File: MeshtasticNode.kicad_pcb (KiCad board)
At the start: 4 copper layers, 71.3 x 72.8 mm, 39 parts, among them J1 Conn_01x02_Socket, J2 Conn_01x02_Socket, J3 Conn_01x04_Socket, J4 Conn_01x03_Pin, J5 Conn_01x03_Pin, J6 Conn_01x03_Pin, J8 Conn_01x03_Pin, U1 BQ24074, U2 HT-CT62, U8 XC6206PxxxMR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

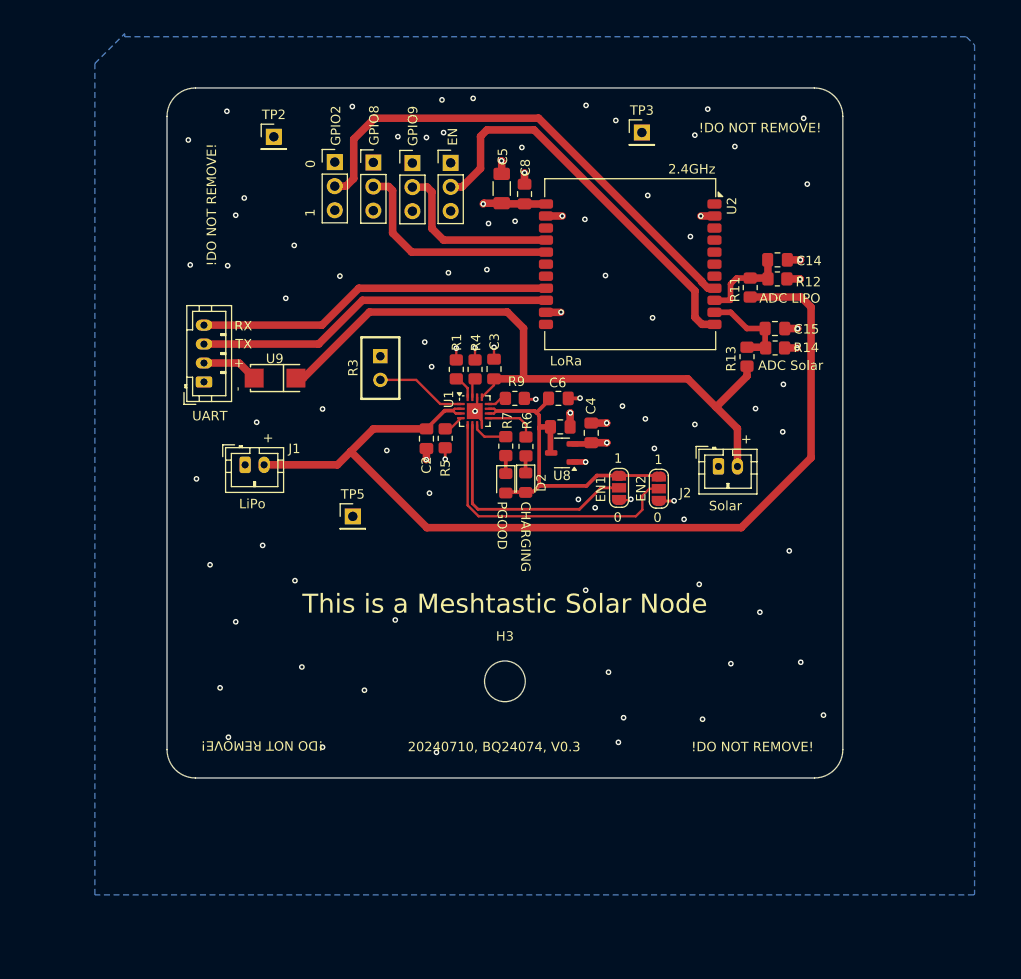
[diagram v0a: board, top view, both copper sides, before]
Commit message: pcb: add I2C port and remove a few warnings from EN1/EN2 solder switches
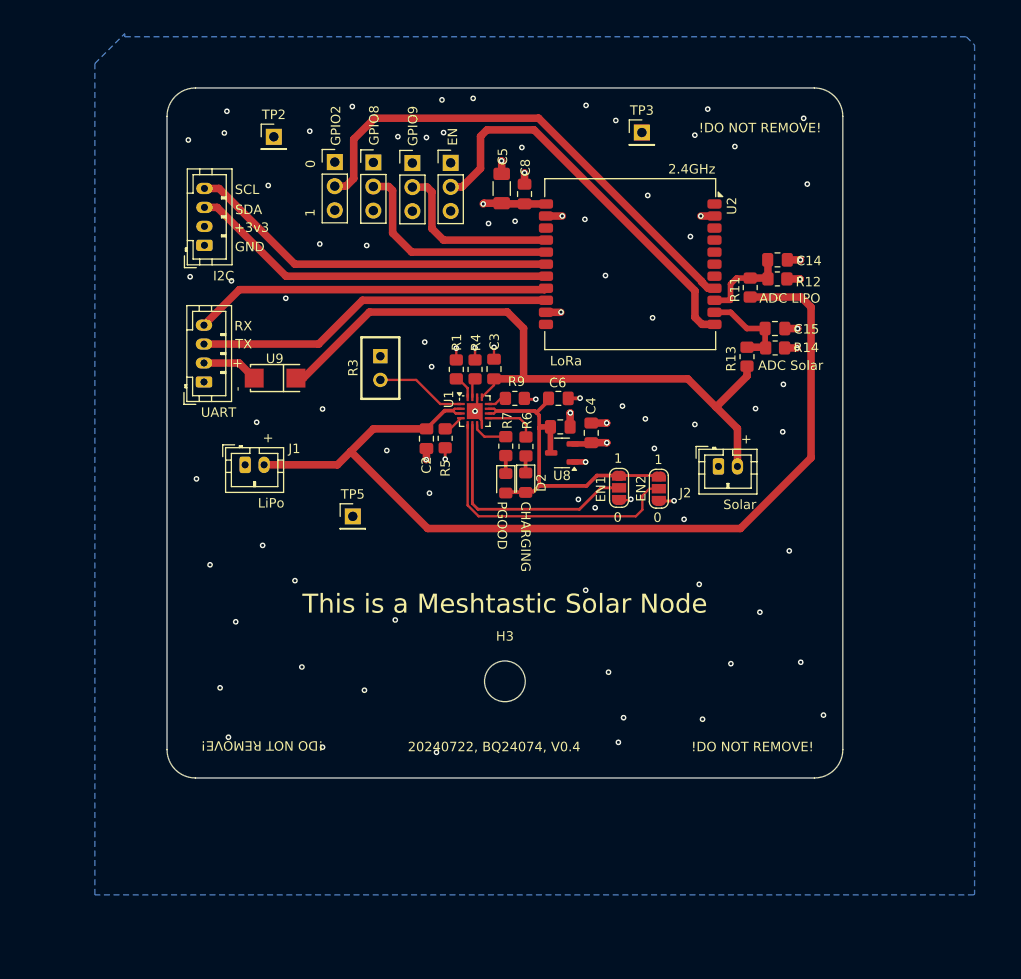
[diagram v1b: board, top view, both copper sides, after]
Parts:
- added J7: Conn_01x04_Socket, Connector_JST:JST_PH_B4B-PH-K_1x04_P2.00mm_Vertical, F.Cu at (187.1, 45.9)
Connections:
- U2 pad 17: /USB_D- -> /I2C_SCL
- U2 pad 18: /USB_D+ -> /I2C_SDA
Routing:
- net /I2C_SCL: track 0.00 -> 39.3 mm
- net /I2C_SDA: track 0.00 -> 39.0 mm
- net GND: vias 93 -> 92
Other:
- board text added: "+3v3"
- board text added: "20240722, BQ24074, V0.4"
- board text added: "GND"
- board text added: "I2C"
- board text added: "SCL"
- board text added: "SDA"
- board text removed: "20240710, BQ24074, V0.3"

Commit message: pcb: add lost front and back groundplane, use thermal via footprint for BQ24074
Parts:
- U1: footprint Package_DFN_QFN:VQFN-16-1EP_3x3mm_P0.5mm_EP1.68x1.68mm -> Package_DFN_QFN:VQFN-16-1EP_3x3mm_P0.5mm_EP1.68x1.68mm_ThermalVias
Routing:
- net GND: vias 92 -> 111
- added copper zone on F.Cu, net GND
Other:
- board text added: "20240802, BQ24074, V0.5"
- board text removed: "20240722, BQ24074, V0.4"

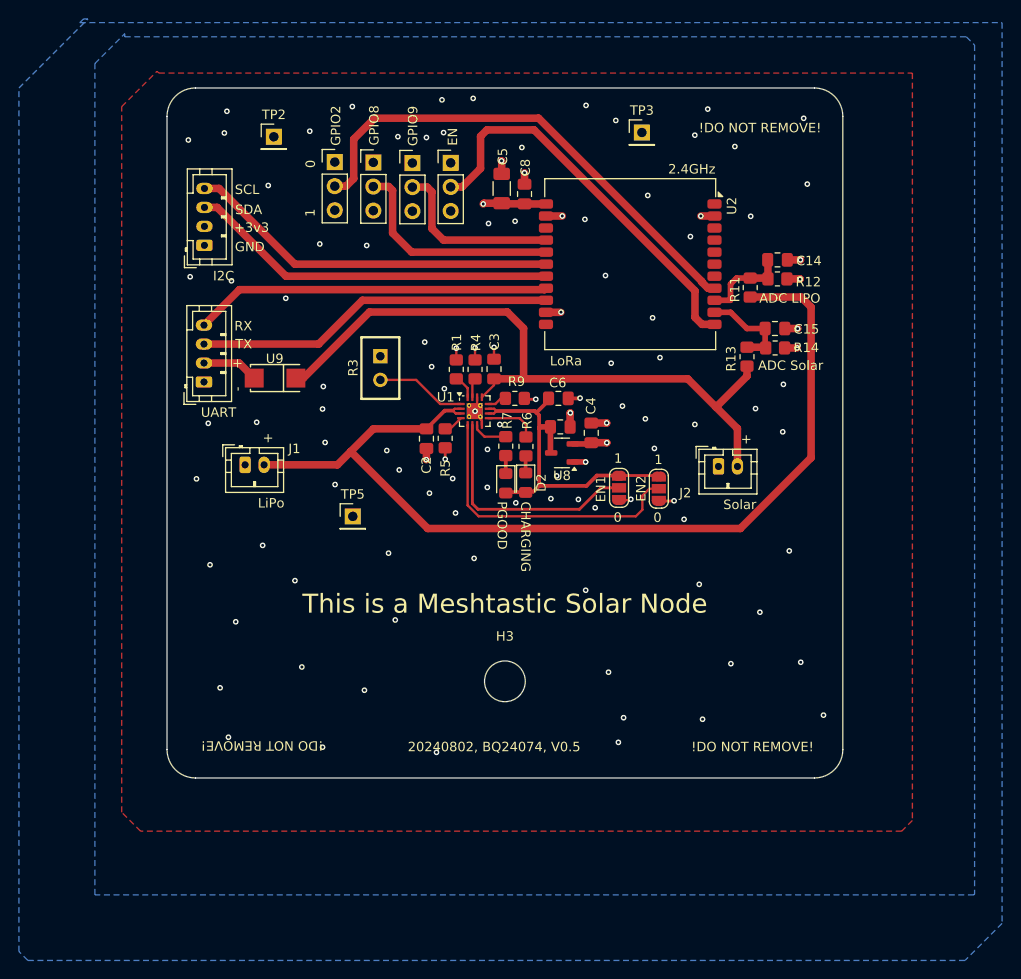
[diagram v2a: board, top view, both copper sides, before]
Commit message: pcb: smaller non-functional cleanups of the design
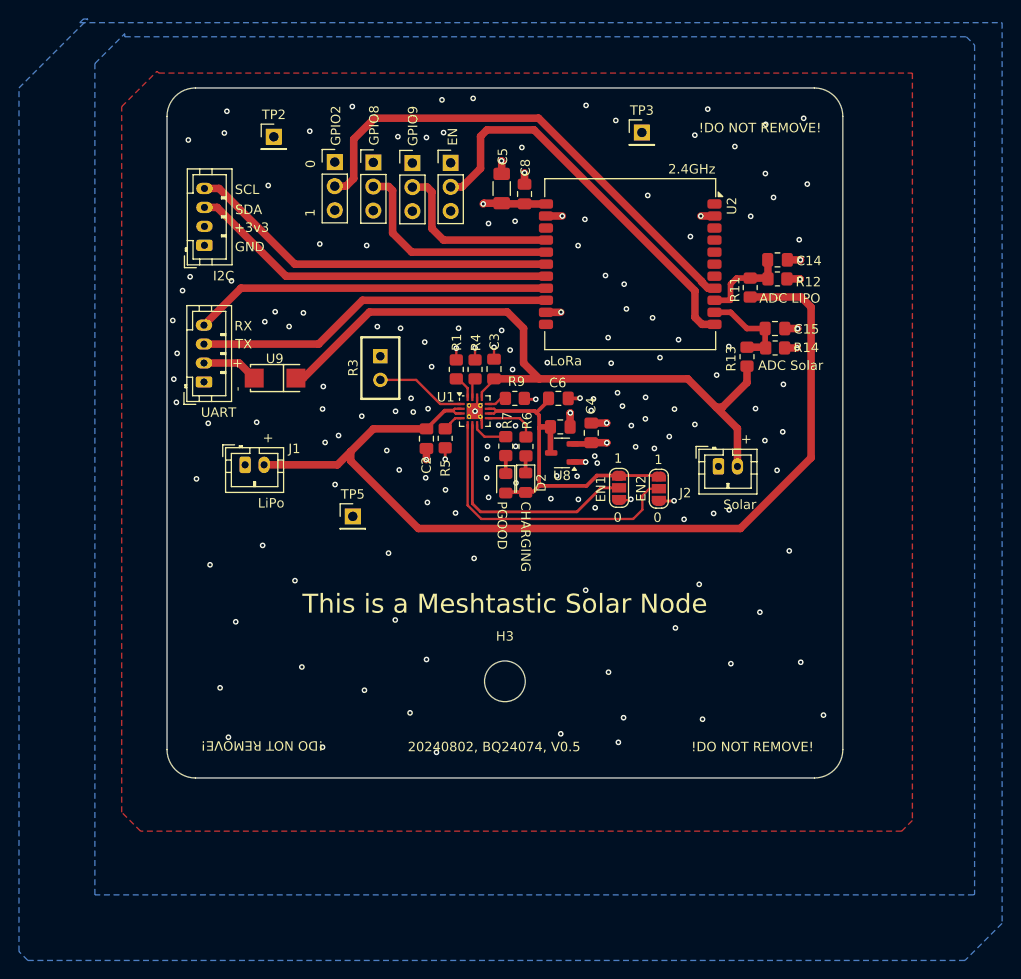
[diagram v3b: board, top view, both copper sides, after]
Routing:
- net /VBUS: track 72.6 -> 74.0 mm
- net /VLIPO: track 102.0 -> 102.5 mm
- net GND: vias 111 -> 166

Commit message: pcb: smaller non-functional cleanups
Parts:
- moved J1 2.92 mm to (194.3, 69.1)
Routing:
- net /VLIPO: track 102.5 -> 99.6 mm
- net GND: vias 166 -> 173
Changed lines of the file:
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@@
 			)
 		)
+		(model "${KICAD8_3DMODEL_DIR}/Package_DFN_QFN.3dshapes/QFN-16-1EP_3x3mm_P0.5mm_EP1.8x1.8mm.step"
+			(offset
+				(xyz 0 0 0)
+			)
+			(scale
+				(xyz 1 1 1)
+			)
+			(rotate
+				(xyz 0 0 0)
+			)
+		)
 	)
 	(footprint "Resistor_SMD:R_0805_2012Metric_Pad1.20x1.40mm_HandSolder"
@@
 	(footprint "Connector_JST:JST_PH_B2B-PH-K_1x02_P2.00mm_Vertical"
 		(layer "F.Cu")
-		(at 191.34 69.06)
+		(at 194.26 69.11)
 		(descr "JST PH series connector, B2B-PH-K (http://www.jst-mfg.com/product/pdf/eng/ePH.pdf), generated with kicad-footprint-generator")
 		(tags "connector JST PH side entry")
@@
 	)
 	(gr_text "+"
-		(at 193.19 66.8 0)
+		(at 195.64 66.88 0)
 		(layer "F.SilkS")
 		(effects
@@
 		(layer "User.3")
 		(pts
+			(xy 183.22 71.7) (xy 195.32 71.7)
+		)
+		(height 0)
+		(gr_text "12.1000 mm"
+			(at 189.27 70.55 0)
+			(layer "User.3")
+			(effects
+				(font
+					(size 1 1)
+					(thickness 0.15)
+				)
+			)
+		)
+		(format
+			(prefix "")
+			(suffix "")
+			(units 2)
+			(units_format 1)
+			(precision 4)
+		)
+		(style
+			(thickness 0.15)
+			(arrow_length 1.27)
+			(text_position_mode 0)
+			(extension_height 0.58642)
+			(extension_offset 0.5) keep_text_aligned)
+	)
+	(dimension
+		(type aligned)
+		(layer "User.3")
+		(pts
+			(xy 254.39 71.7) (xy 242.28 71.7)
+		)
+		(height 0)
+		(gr_text "12.1100 mm"
+			(at 248.335 70.55 0)
+			(layer "User.3")
+			(effects
+				(font
+					(size 1 1)
+					(thickness 0.15)
+				)
+			)
+		)
+		(format
+			(prefix "")
+			(suffix "")
+			(units 2)
+			(units_format 1)
+			(precision 4)
+		)
+		(style
+			(thickness 0.15)
+			(arrow_length 1.27)
+			(text_position_mode 0)
+			(extension_height 0.58642)
+			(extension_offset 0.5) keep_text_aligned)
+	)
+	(dimension
+		(type aligned)
+		(layer "User.3")
+		(pts
 			(xy 218.75 84.9) (xy 183.1 84.9)
 		)
@@
 	)
 	(via
+		(at 242.6 54.76)
+		(size 0.4)
+		(drill 0.2)
+		(layers "F.Cu" "B.Cu")
+		(free yes)
+		(net 2)
+	)
+	(via
 		(at 211.53 99.39)
 		(size 0.6)
@@
 	)
 	(via
+		(at 248.27 52.86)
+		(size 0.4)
+		(drill 0.2)
+		(layers "F.Cu" "B.Cu")
+		(free yes)
+		(net 2)
+	)
+	(via
 		(at 196.6 81.28)
 		(size 0.6)
@@
 	)
 	(via
+		(at 249.84 53)
+		(size 0.4)
+		(drill 0.2)
+		(layers "F.Cu" "B.Cu")
+		(free yes)
+		(net 2)
+	)
+	(via
 		(at 210.47 34.53)
 		(size 0.6)
@@
 	)
 	(via
+		(at 244.53 53.05)
+		(size 0.4)
+		(drill 0.2)
+		(layers "F.Cu" "B.Cu")
+		(free yes)
+		(net 2)
+	)
+	(via
 		(at 229.68 90.94)
 		(size 0.6)
@@
 	)
 	(via
+		(at 245.82 53.11)
+		(size 0.4)
+		(drill 0.2)
+		(layers "F.Cu" "B.Cu")
+		(free yes)
+		(net 2)
+	)
+	(via
 		(at 215.599998 56.717501)
 		(size 0.6)
@@
 	)
 	(via
+		(at 243.79 52.7)
+		(size 0.4)
+		(drill 0.2)
+		(layers "F.Cu" "B.Cu")
+		(free yes)
+		(net 2)
+	)
+	(via
 		(at 238.32 44.98)
 		(size 0.6)
@@
 	)
 	(via
+		(at 243.26 55.33)
+		(size 0.4)
+		(drill 0.2)
+		(layers "F.Cu" "B.Cu")
+		(free yes)
+		(net 2)
+	)
+	(via
 		(at 218.41 54.88)
 		(size 0.6)
@@
 	)
 	(segment
-		(start 202.485 67.655)
-		(end 201.08 69.06)
+		(start 196.37 69.06)
+		(end 196.33 69.1)
 		(width 0.8)
 		(layer "F.Cu")
@@
 	)
 	(segment
-		(start 201.08 69.06)
-		(end 193.34 69.06)
+		(start 251.05 52.42)
+		(end 251.05 68.32)
 		(width 0.8)
 		(layer "F.Cu")
@@
 	)
 	(segment
-		(start 251.05 52.42)
-		(end 251.05 68.32)
+		(start 243.59 75.78)
+		(end 209.62 75.78)
 		(width 0.8)
 		(layer "F.Cu")
@@
 	)
 	(segment
-		(start 243.59 75.78)
-		(end 209.62 75.78)
+		(start 201.08 69.06)
+		(end 196.37 69.06)
 		(width 0.8)
 		(layer "F.Cu")
@@
 	)
 	(segment
+		(start 202.485 67.655)
+		(end 201.08 69.06)
+		(width 0.8)
+		(layer "F.Cu")
+		(net 3)
+	)
+	(segment
 		(start 202.485 68.645)
 		(end 202.485 67.655)
@@
 		(polygon
 			(pts
-				(xy 249.7 52.12) (xy 243.7 52.12) (xy 243.7 53.13) (xy 244.26 53.69) (xy 247.19 53.69) (xy 247.24 53.64)
-				(xy 249.55 53.64) (xy 249.76 53.85) (xy 249.94 53.67) (xy 249.94 52.34) (xy 249.7 52.1)
+				(xy 209 66.45) (xy 213.18 66.45) (xy 214.28 67.55) (xy 214.28 68.09) (xy 211.86 68.09) (xy 211.74 67.97)
+				(xy 209.43 67.97) (xy 209.04 67.58) (xy 209.04 66.51) (xy 209.03 66.51) (xy 209 66.48)
 			)
 		)
@@
 		(net 0)
 		(net_name "")
-		(layer "F.Cu")
-		(hatch edge 0.5)
+		(layers "F.Cu" "Edge.Cuts")
+		(hatch full 0.5)
 		(connect_pads
 			(clearance 0)
 		)
-		(min_thickness 0.26)
+		(min_thickness 0.25)
 		(filled_areas_thickness no)
 		(keepout
@@
 		(polygon
 			(pts
-				(xy 209 66.45) (xy 213.18 66.45) (xy 214.28 67.55) (xy 214.28 68.09) (xy 211.86 68.09) (xy 211.74 67.97)
-				(xy 209.43 67.97) (xy 209.04 67.58) (xy 209.04 66.51) (xy 209.03 66.51) (xy 209 66.48)
+				(xy 224.02 62.59) (xy 226.55 62.59) (xy 226.98 63.02) (xy 226.98 69.69) (xy 226.85 69.82) (xy 222.56 69.82)
+				(xy 222.56 64.05)
 			)
 		)
@@
 		(net_name "")
 		(layers "F.Cu" "Edge.Cuts")
-		(hatch full 0.5)
+		(hatch edge 0.5)
 		(connect_pads
 			(clearance 0)
@@
 		(polygon
 			(pts
-				(xy 224.02 62.59) (xy 226.55 62.59) (xy 226.98 63.02) (xy 226.98 69.69) (xy 226.85 69.82) (xy 222.56 69.82)
-				(xy 222.56 64.05)
+				(xy 242.92 48.41) (xy 245.8 48.41) (xy 245.6 48.61) (xy 245.6 46.14) (xy 248.99 46.14) (xy 249.44 46.59)
+				(xy 249.44 50.56) (xy 249.13 50.87) (xy 245.72 50.87) (xy 245.72 52.34) (xy 245.71 52.35) (xy 243.62 52.35)
+				(xy 242.82 52.15)
 			)
 		)
